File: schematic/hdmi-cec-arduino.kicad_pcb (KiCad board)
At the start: 2 copper layers, 68.6 x 53.3 mm, 26 parts, among them J1 Power, J2 Digital/PWM, J3 Analog, J4 Digital/PWM, J5 HDMI_A, J6 HDMI_A, J7 Conn_01x03, J8 Conn_01x02, Q1 BC847, Q2 BC847

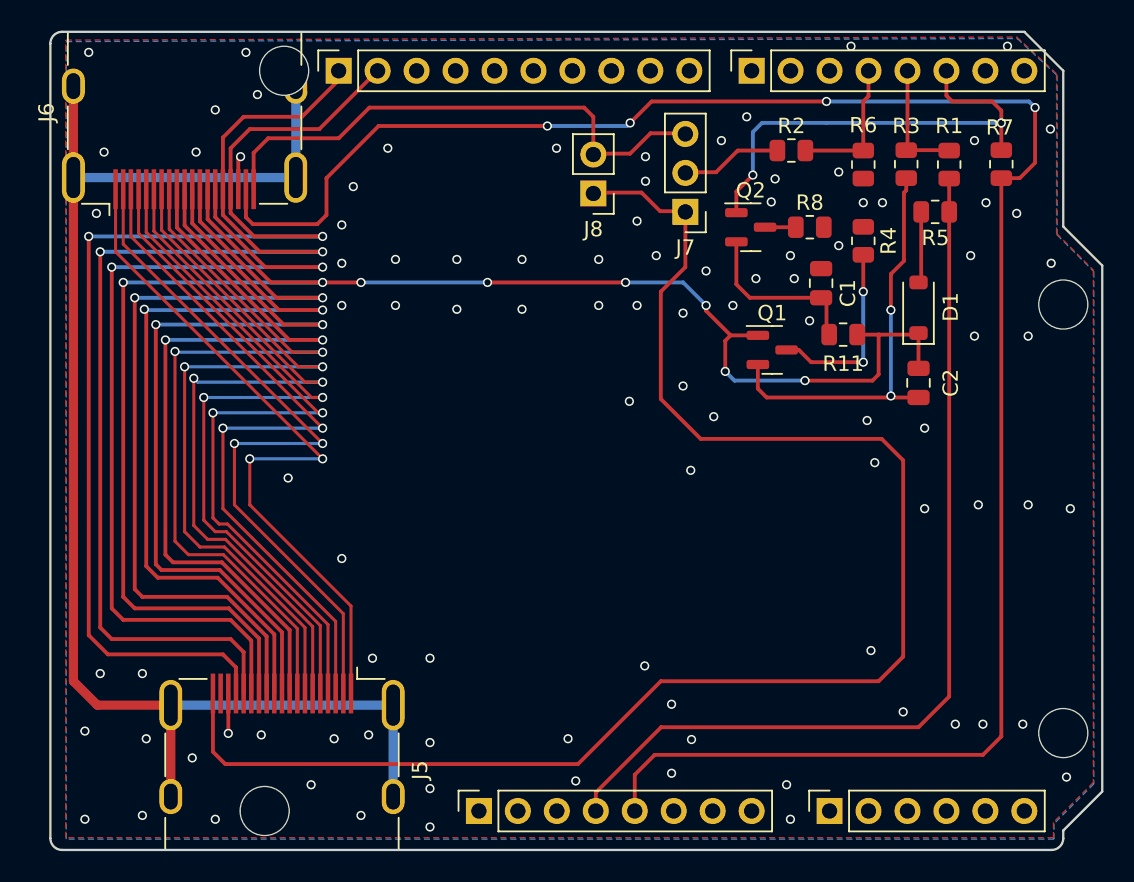
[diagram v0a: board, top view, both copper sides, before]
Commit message: Ready for production with Molex HDMI
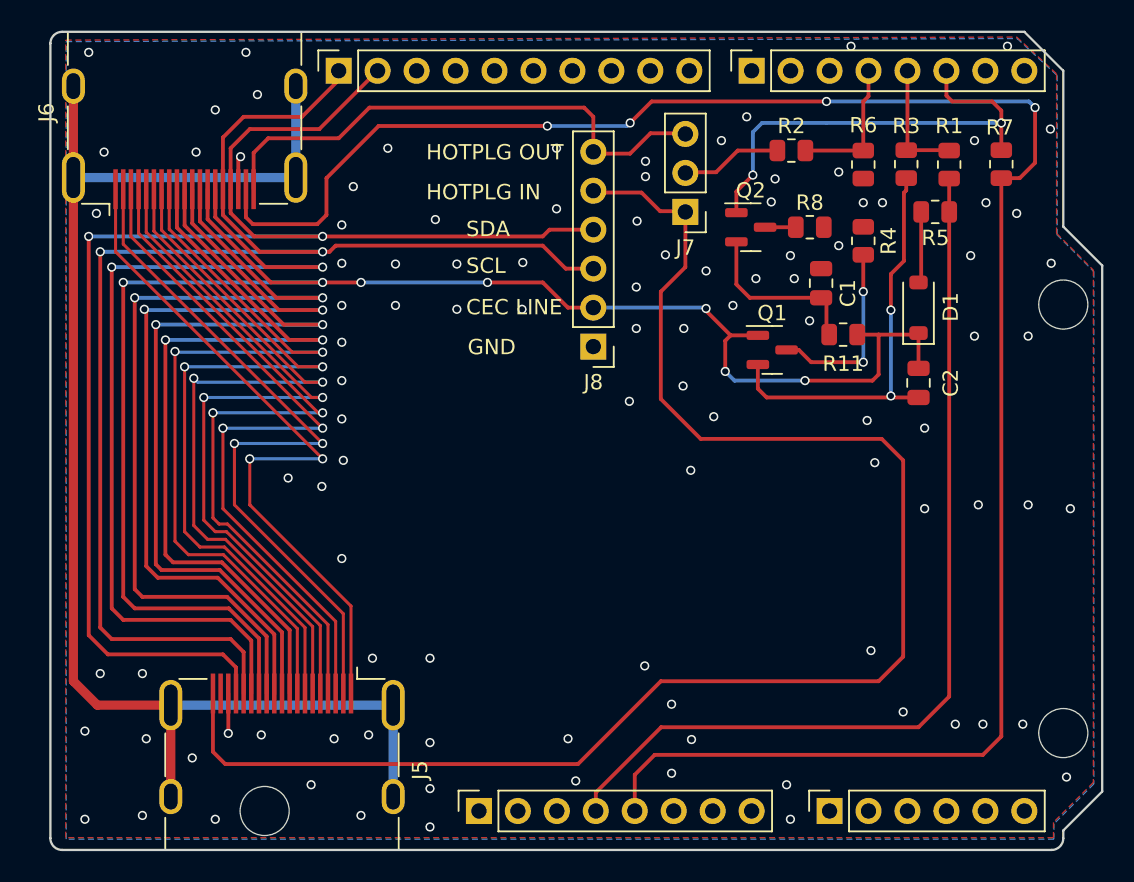
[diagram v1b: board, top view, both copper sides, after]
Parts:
- removed MH1: MountingHole_3.2mm, Arduino_MountingHole:MountingHole_3.2mm
- J8: value Conn_01x02 -> Conn_01x06; footprint Connector_PinHeader_2.54mm:PinHeader_1x02_P2.54mm_Vertical -> Connector_PinHeader_2.54mm:PinHeader_1x06_P2.54mm_Vertical
- moved J8 9.98 mm to (135.4, 67.2)
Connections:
- J8 pad 1: /HPD_IN -> GND
- J8 pad 2: /HPD_OUT -> /CEC_LINE
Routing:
- net SCL: track 74.0 -> 92.4 mm
- net SDA: track 76.0 -> 93.8 mm
- net /CEC_LINE: track 110.1 -> 109.8 mm, vias 8 -> 7
- net GND: vias 98 -> 104
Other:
- board text added: "CEC LINE"
- board text added: "GND"
- board text added: "HOTPLG IN"
- board text added: "HOTPLG OUT"
- board text added: "SCL"
- board text added: "SDA"

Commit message: Re-Place HDMI connectors and add solder jumper for some signals
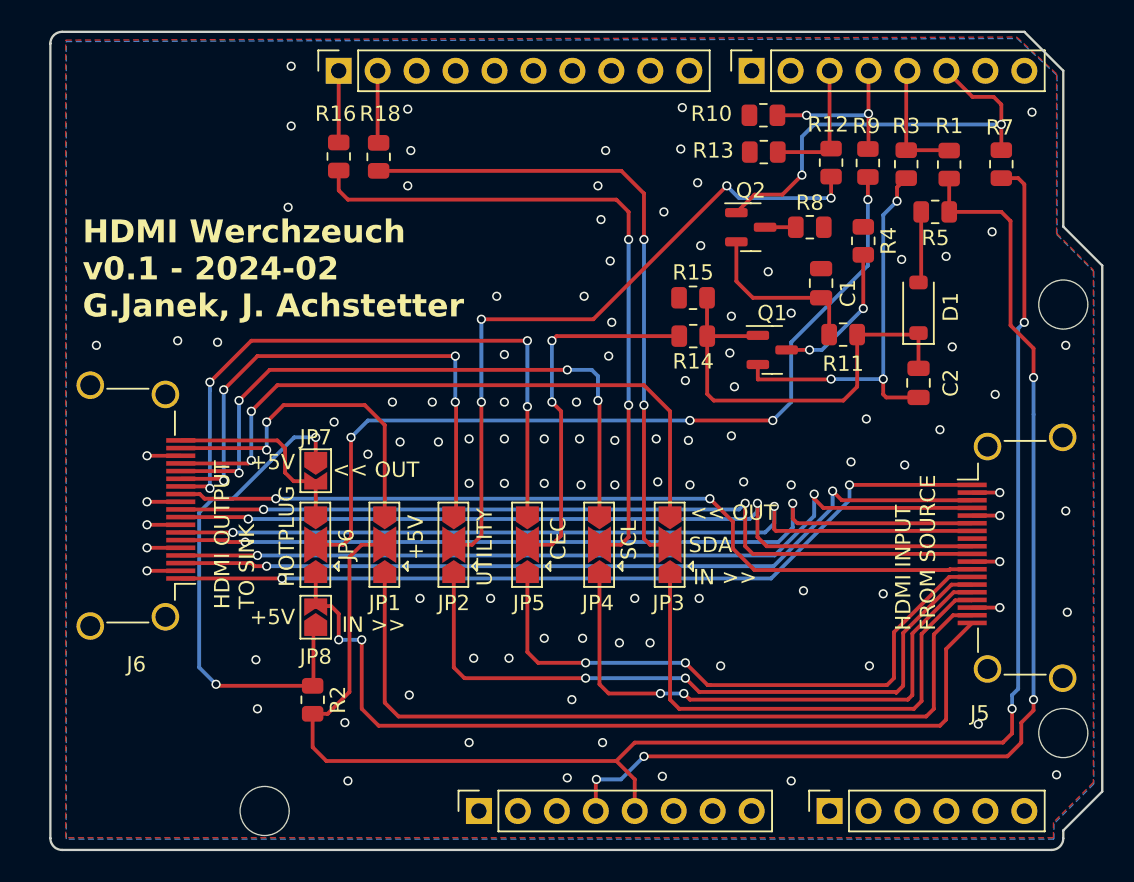
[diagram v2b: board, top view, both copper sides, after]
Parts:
- removed J7: Conn_01x03, Connector_PinHeader_2.54mm:PinHeader_1x03_P2.54mm_Vertical
- removed J8: Conn_01x06, Connector_PinHeader_2.54mm:PinHeader_1x06_P2.54mm_Vertical
- removed R6: 100k, Resistor_SMD:R_0805_2012Metric
- added JP1: SolderJumper_3_Open, Jumper:SolderJumper-3_P2.0mm_Open_TrianglePad1.0x1.5mm, F.Cu at (121.8, 80.1)
- added JP2: SolderJumper_3_Open, Jumper:SolderJumper-3_P2.0mm_Open_TrianglePad1.0x1.5mm, F.Cu at (126.3, 80.1)
- added JP3: SolderJumper_3_Open, Jumper:SolderJumper-3_P2.0mm_Open_TrianglePad1.0x1.5mm, F.Cu at (140.4, 80.1)
- added JP4: SolderJumper_3_Open, Jumper:SolderJumper-3_P2.0mm_Open_TrianglePad1.0x1.5mm, F.Cu at (135.8, 80.1)
- added JP5: SolderJumper_3_Open, Jumper:SolderJumper-3_P2.0mm_Open_TrianglePad1.0x1.5mm, F.Cu at (131.1, 80.1)
- added JP6: SolderJumper_3_Open, Jumper:SolderJumper-3_P2.0mm_Open_TrianglePad1.0x1.5mm, F.Cu at (117.3, 80.1)
- added JP7: SolderJumper_2_Open, Jumper:SolderJumper-2_P1.3mm_Open_TrianglePad1.0x1.5mm, F.Cu at (117.3, 75.3)
- added JP8: SolderJumper_2_Open, Jumper:SolderJumper-2_P1.3mm_Open_TrianglePad1.0x1.5mm, F.Cu at (117.3, 84.8)
- added R10: 100k, Resistor_SMD:R_0805_2012Metric, F.Cu at (146.5, 52.1)
- added R12: 220R, Resistor_SMD:R_0805_2012Metric, F.Cu at (150.9, 55.2)
- added R13: 100k, Resistor_SMD:R_0805_2012Metric, F.Cu at (146.5, 54.5)
- added R14: 220R, Resistor_SMD:R_0805_2012Metric, F.Cu at (141.9, 66.5)
- added R15: 100k, Resistor_SMD:R_0805_2012Metric, F.Cu at (141.9, 64.0)
- added R16: 220R, Resistor_SMD:R_0805_2012Metric, F.Cu at (118.8, 54.8)
- added R18: 220R, Resistor_SMD:R_0805_2012Metric, F.Cu at (121.4, 54.8)
- added R9: 220R, Resistor_SMD:R_0805_2012Metric, F.Cu at (153.3, 55.2)
- J5, J6: footprint Connector_HDMI:HDMI_A_Molex_208658-1001_Horizontal -> Connector_HDMI:HDMI_A_Amphenol_10029449-x01xLF_Horizontal
- R2: value 220R -> 1k
- moved J5 51.5 mm to (165.1, 81.0), turned to 90 degrees
- moved R2 47.5 mm to (117.1, 90.2), turned to -90 degrees
- moved J6 24.5 mm to (103.5, 77.5), turned to -90 degrees
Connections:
- net Net-(J5-CK+) renamed /CK+
- net Net-(J5-CK-) renamed /CK-
- net Net-(J5-D0+) renamed /D0+
- net Net-(J5-D0-) renamed /D0-
- net Net-(J5-D1+) renamed /D1+
- net Net-(J5-D1-) renamed /D1-
- net Net-(J5-D2+) renamed /D2+
- net Net-(J5-D2-) renamed /D2-
- J2 pad 1: SCL -> /SCL/A5
- J2 pad 2: SDA -> /SDA/A4
- J5 pad 11: Net-(J5-CKS) -> GND
- J5 pad 13: /CEC_LINE -> /CEC_IN
- J5 pad 14: Net-(J5-UTILITY) -> /UTILITY_IN
- J5 pad 15: SCL -> /SCL_IN
- J5 pad 16: SDA -> /SDA_IN
- J5 pad 18: unconnected-(J5-+5V-Pad18) -> /5V_IN
- J5 pad 2: Net-(J5-D2S) -> GND
- J5 pad 5: Net-(J5-D1S) -> GND
- J5 pad 8: Net-(J5-D0S) -> GND
- J5 pad SH: Net-(J5-PadSH) -> GND
- J6 pad 11: Net-(J5-CKS) -> GND
- J6 pad 13: /CEC_LINE -> /CEC_OUT
- J6 pad 14: Net-(J5-UTILITY) -> /UTILITY_OUT
- J6 pad 15: SCL -> /SCL_OUT
- J6 pad 16: SDA -> /SDA_OUT
- J6 pad 18: +5V -> /5V_OUT
- J6 pad 2: Net-(J5-D2S) -> GND
- J6 pad 5: Net-(J5-D1S) -> GND
- J6 pad 8: Net-(J5-D0S) -> GND
- J6 pad SH: Net-(J5-PadSH) -> GND
- R2 pad 1: /4 -> Net-(JP7-A)
- R2 pad 2: Net-(J7-Pin_2) -> +5V
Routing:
- net SDA: track 93.8 -> 0.00 mm, vias 2 -> 0
- net Net-(J5-PadSH): track 92.4 -> 0.00 mm
- net SCL: track 92.4 -> 0.00 mm, vias 2 -> 0
- net /CEC_LINE: track 109.8 -> 29.7 mm, vias 7 -> 0
- net Net-(J5-UTILITY): track 59.6 -> 0.00 mm, vias 2 -> 0
- net Net-(J5-CKS): track 55.6 -> 0.00 mm, vias 2 -> 0
- net Net-(JP6-C): track 0.00 -> 55.4 mm, vias 0 -> 4
- net /5V_IN: track 0.00 -> 52.5 mm
- net Net-(J5-D0S): track 52.5 -> 0.00 mm, vias 2 -> 0
- net Net-(J5-D1S): track 49.4 -> 0.00 mm, vias 2 -> 0
- net Net-(J5-D2S): track 47.0 -> 0.00 mm, vias 2 -> 0
- net /UTILITY_IN: track 0.00 -> 45.6 mm, vias 0 -> 2
- net /HPD_IN: track 101.7 -> 57.1 mm, vias 0 -> 2
- net Net-(JP2-C): track 0.00 -> 44.3 mm, vias 0 -> 4
- net Net-(JP4-C): track 0.00 -> 44.1 mm, vias 0 -> 2
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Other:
- board text added: "+5V"
- board text added: "<< OUT"
- board text added: "CEC"
- board text added: "HDMI INPUT FROM SOURCE"
- board text added: "HDMI OUTPUT TO SINK"
- board text added: "HDMI Werchzeuch v0.1 - 2024-02 G.Janek, J. Achstetter"
- board text added: "HOTPLUG"
- board text added: "IN >>"
- board text added: "UTILITY"
- board text removed: "CEC LINE"
- board text removed: "GND"
- board text removed: "HOTPLG IN"
- board text removed: "HOTPLG OUT"
